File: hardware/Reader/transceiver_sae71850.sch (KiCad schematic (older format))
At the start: 17 parts

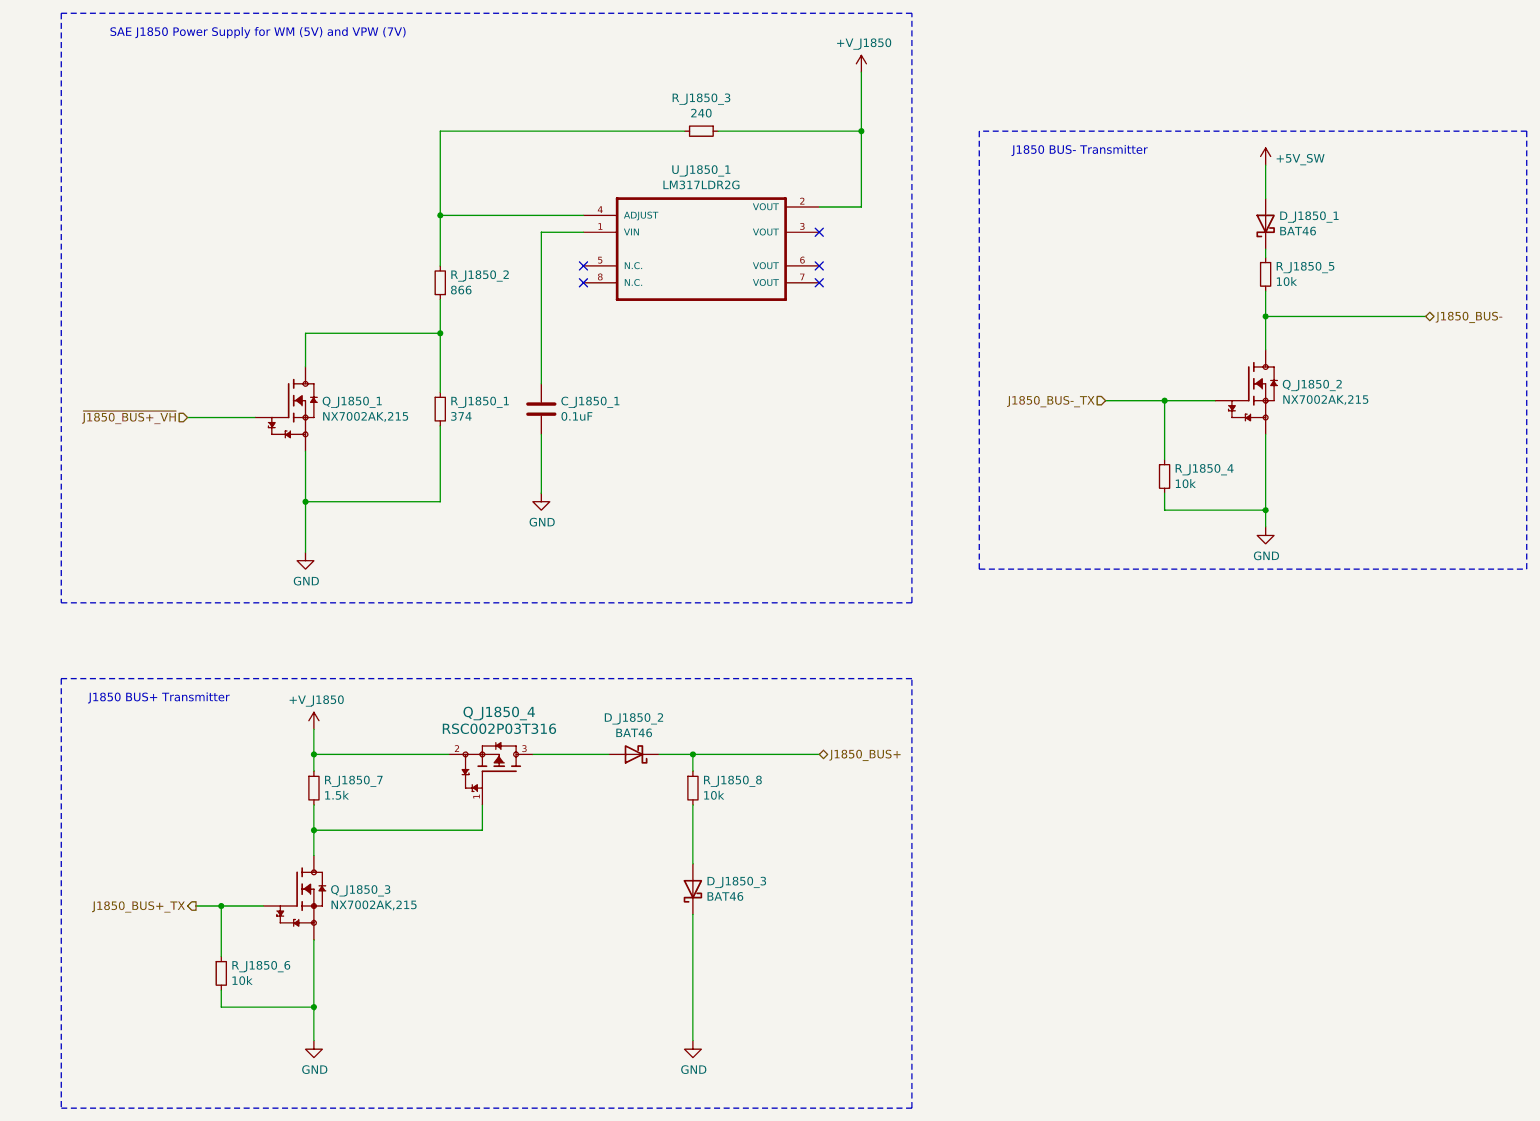
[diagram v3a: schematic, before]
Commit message: Fixed wiring issue on ESD Protection
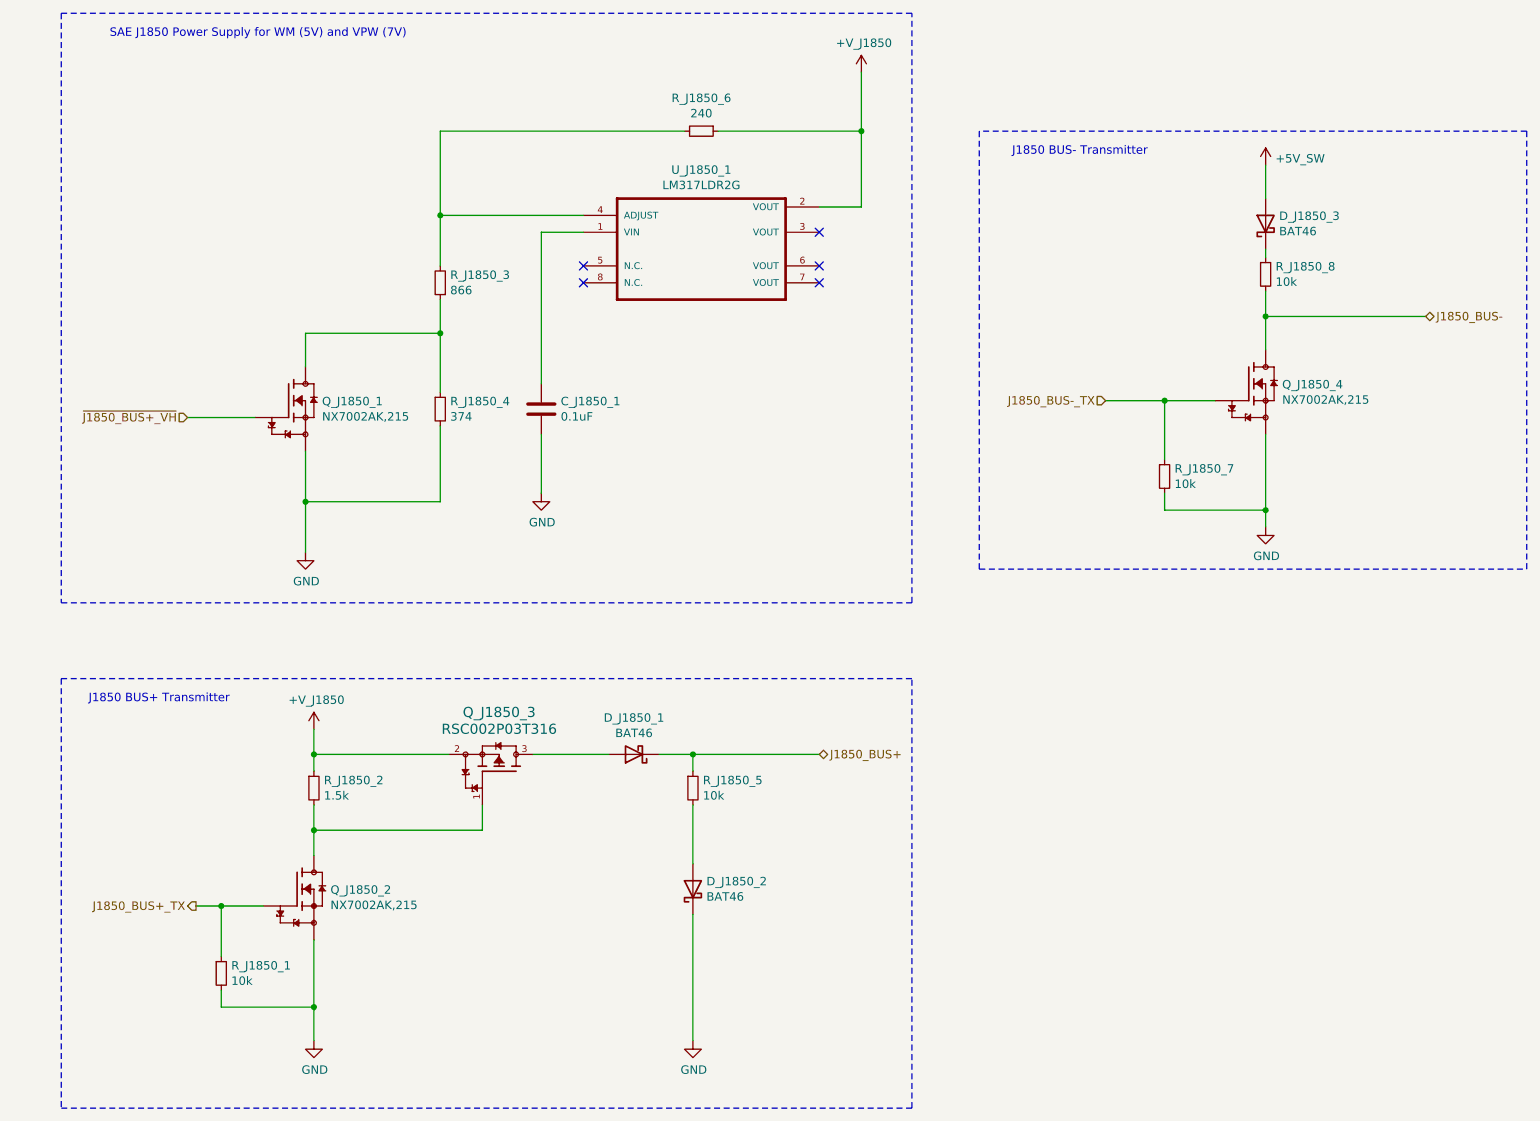
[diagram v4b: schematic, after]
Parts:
- renumbered D_J1850_2 to D_J1850_1, D_J1850_3 to D_J1850_2, D_J1850_1 to D_J1850_3, Q_J1850_3 to Q_J1850_2, Q_J1850_4 to Q_J1850_3, Q_J1850_2 to Q_J1850_4, R_J1850_6 to R_J1850_1, R_J1850_7 to R_J1850_2, R_J1850_2 to R_J1850_3, R_J1850_1 to R_J1850_4, R_J1850_8 to R_J1850_5, R_J1850_3 to R_J1850_6, R_J1850_4 to R_J1850_7, R_J1850_5 to R_J1850_8
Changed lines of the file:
@@
 $EndComp
 $Comp
-L power:GND #PWR0165
+L power:GND #PWR032
 U 1 1 5FB553C7
 P 3500 3550
-F 0 "#PWR0165" H 3500 3300 50  0001 C CNN
+F 0 "#PWR032" H 3500 3300 50  0001 C CNN
 F 1 "GND" H 3505 3377 50  0000 C CNN
 F 2 "" H 3500 3550 50  0001 C CNN
@@
 $EndComp
 $Comp
-L Device:R_Small R_J1850_3
+L Device:R_Small R_J1850_6
 U 1 1 5FB55A16
 P 4450 1400
-F 0 "R_J1850_3" V 4254 1400 50  0000 C CNN
+F 0 "R_J1850_6" V 4254 1400 50  0000 C CNN
 F 1 "240" V 4345 1400 50  0000 C CNN
 F 2 "footprints:RESC3216X70N" H 4450 1400 50  0001 C CNN
@@
 $EndComp
 $Comp
-L Device:R_Small R_J1850_2
+L Device:R_Small R_J1850_3
 U 1 1 5FB56090
 P 2900 2300
-F 0 "R_J1850_2" H 2841 2254 50  0000 R CNN
+F 0 "R_J1850_3" H 2841 2254 50  0000 R CNN
 F 1 "866" H 2841 2345 50  0000 R CNN
 F 2 "footprints:RESC3216X70N" H 2900 2300 50  0001 C CNN
@@
 $EndComp
 $Comp
-L Device:R_Small R_J1850_1
+L Device:R_Small R_J1850_4
 U 1 1 5FB59A27
 P 2900 3050
-F 0 "R_J1850_1" H 2959 3096 50  0000 L CNN
+F 0 "R_J1850_4" H 2959 3096 50  0000 L CNN
 F 1 "374" H 2959 3005 50  0000 L CNN
 F 2 "footprints:RESC3216X70N" H 2900 3050 50  0001 C CNN
@@
 	2900 3600 2900 3150
 $Comp
-L power:GND #PWR0166
+L power:GND #PWR029
 U 1 1 5FB5A98F
 P 2100 3900
-F 0 "#PWR0166" H 2100 3650 50  0001 C CNN
+F 0 "#PWR029" H 2100 3650 50  0001 C CNN
 F 1 "GND" H 2105 3727 50  0000 C CNN
 F 2 "" H 2100 3900 50  0001 C CNN
@@
 Connection ~ 2100 3600
 $Comp
-L CANtech:+V_J1850 #PWR0167
+L CANtech:+V_J1850 #PWR034
 U 1 1 5FB539A6
 P 5400 1050
-F 0 "#PWR0167" H 5400 900 50  0001 C CNN
+F 0 "#PWR034" H 5400 900 50  0001 C CNN
 F 1 "+V_J1850" H 5415 1223 50  0000 C CNN
 F 2 "" H 5400 1050 50  0001 C CNN
@@
 SAE J1850 Power Supply for WM (5V) and VPW (7V)
 $Comp
-L NX7002AK_215:NX7002AK,215 Q_J1850_3
+L NX7002AK_215:NX7002AK,215 Q_J1850_2
 U 1 1 5FB62A81
 P 2050 5900
-F 0 "Q_J1850_3" H 2248 5896 50  0000 L CNN
+F 0 "Q_J1850_2" H 2248 5896 50  0000 L CNN
 F 1 "NX7002AK,215" H 2248 5805 50  0000 L CNN
 F 2 "footprints:SOT95P230X110-3N" H 2050 5900 50  0001 L BNN
@@
 $EndComp
 $Comp
-L RSC002P03T316:RSC002P03T316 Q_J1850_4
+L RSC002P03T316:RSC002P03T316 Q_J1850_3
 U 1 1 5FB63A72
 P 3000 5450
-F 0 "Q_J1850_4" V 3600 5700 60  0000 C CNN
+F 0 "Q_J1850_3" V 3600 5700 60  0000 C CNN
 F 1 "RSC002P03T316" V 3500 5700 60  0000 C CNN
 F 2 "footprints:RSC002P03T316" H 3800 5690 60  0001 C CNN
@@
 $EndComp
 $Comp
-L Device:R_Small R_J1850_7
+L Device:R_Small R_J1850_2
 U 1 1 5FB64FDA
 P 2150 5300
-F 0 "R_J1850_7" H 2209 5346 50  0000 L CNN
+F 0 "R_J1850_2" H 2209 5346 50  0000 L CNN
 F 1 "1.5k" H 2209 5255 50  0000 L CNN
 F 2 "footprints:RESC1607X60N" H 2150 5300 50  0001 C CNN
@@
 	2150 5200 2150 5100
 $Comp
-L CANtech:+V_J1850 #PWR0168
+L CANtech:+V_J1850 #PWR030
 U 1 1 5FB735C3
 P 2150 4950
-F 0 "#PWR0168" H 2150 4800 50  0001 C CNN
+F 0 "#PWR030" H 2150 4800 50  0001 C CNN
 F 1 "+V_J1850" H 2165 5123 50  0000 C CNN
 F 2 "" H 2150 4950 50  0001 C CNN
@@
 J1850_BUS+_TX
 $Comp
-L Device:R_Small R_J1850_6
+L Device:R_Small R_J1850_1
 U 1 1 5FB73FCF
 P 1600 6400
-F 0 "R_J1850_6" H 1659 6446 50  0000 L CNN
+F 0 "R_J1850_1" H 1659 6446 50  0000 L CNN
 F 1 "10k" H 1659 6355 50  0000 L CNN
 F 2 "footprints:RESC1608X55N" H 1600 6400 50  0001 C CNN
@@
 $EndComp
 $Comp
-L power:GND #PWR0169
+L power:GND #PWR031
 U 1 1 5FB743BE
 P 2150 6800
-F 0 "#PWR0169" H 2150 6550 50  0001 C CNN
+F 0 "#PWR031" H 2150 6550 50  0001 C CNN
 F 1 "GND" H 2155 6627 50  0000 C CNN
 F 2 "" H 2150 6800 50  0001 C CNN
@@
 Connection ~ 2150 5100
 $Comp
-L Diode:BAT46 D_J1850_2
+L Diode:BAT46 D_J1850_1
 U 1 1 5FB795A0
 P 4050 5100
-F 0 "D_J1850_2" H 4050 4883 50  0000 C CNN
+F 0 "D_J1850_1" H 4050 4883 50  0000 C CNN
 F 1 "BAT46" H 4050 4974 50  0000 C CNN
 F 2 "Diode_THT:D_DO-35_SOD27_P7.62mm_Horizontal" H 4050 4925 50  0001 C CNN
@@
 	4200 5100 4400 5100
 $Comp
-L Device:R_Small R_J1850_8
+L Device:R_Small R_J1850_5
 U 1 1 5FB7CD86
 P 4400 5300
-F 0 "R_J1850_8" H 4459 5346 50  0000 L CNN
+F 0 "R_J1850_5" H 4459 5346 50  0000 L CNN
 F 1 "10k" H 4459 5255 50  0000 L CNN
 F 2 "footprints:RESC1608X55N" H 4400 5300 50  0001 C CNN
@@
 $EndComp
 $Comp
-L Diode:BAT46 D_J1850_3
+L Diode:BAT46 D_J1850_2
 U 1 1 5FB7D020
 P 4400 5900
-F 0 "D_J1850_3" V 4446 5820 50  0000 R CNN
+F 0 "D_J1850_2" V 4446 5820 50  0000 R CNN
 F 1 "BAT46" V 4355 5820 50  0000 R CNN
 F 2 "Diode_THT:D_DO-35_SOD27_P7.62mm_Horizontal" H 4400 5725 50  0001 C CNN
@@
 	4400 5400 4400 5750
 $Comp
-L power:GND #PWR0170
+L power:GND #PWR033
 U 1 1 5FB7EDB5
 P 4400 6800
-F 0 "#PWR0170" H 4400 6550 50  0001 C CNN
+F 0 "#PWR033" H 4400 6550 50  0001 C CNN
 F 1 "GND" H 4405 6627 50  0000 C CNN
 F 2 "" H 4400 6800 50  0001 C CNN
@@
 J1850_BUS-_TX
 $Comp
-L NX7002AK_215:NX7002AK,215 Q_J1850_2
+L NX7002AK_215:NX7002AK,215 Q_J1850_4
 U 1 1 5FB836A9
 P 7700 2900
-F 0 "Q_J1850_2" H 7898 2896 50  0000 L CNN
+F 0 "Q_J1850_4" H 7898 2896 50  0000 L CNN
 F 1 "NX7002AK,215" H 7898 2805 50  0000 L CNN
 F 2 "footprints:SOT95P230X110-3N" H 7700 2900 50  0001 L BNN
@@
 $EndComp
 $Comp
-L Device:R_Small R_J1850_4
+L Device:R_Small R_J1850_7
 U 1 1 5FB84DD1
 P 7200 3450
-F 0 "R_J1850_4" H 7259 3496 50  0000 L CNN
+F 0 "R_J1850_7" H 7259 3496 50  0000 L CNN
 F 1 "10k" H 7259 3405 50  0000 L CNN
 F 2 "footprints:RESC1608X55N" H 7200 3450 50  0001 C CNN
@@
 $EndComp
 $Comp
-L Device:R_Small R_J1850_5
+L Device:R_Small R_J1850_8
 U 1 1 5FB8513E
 P 7800 2250
-F 0 "R_J1850_5" H 7859 2296 50  0000 L CNN
+F 0 "R_J1850_8" H 7859 2296 50  0000 L CNN
 F 1 "10k" H 7859 2205 50  0000 L CNN
 F 2 "footprints:RESC1608X55N" H 7800 2250 50  0001 C CNN
@@
 $EndComp
 $Comp
-L Diode:BAT46 D_J1850_1
+L Diode:BAT46 D_J1850_3
 U 1 1 5FB86936
 P 7800 1950
-F 0 "D_J1850_1" V 7846 1870 50  0000 R CNN
+F 0 "D_J1850_3" V 7846 1870 50  0000 R CNN
 F 1 "BAT46" V 7755 1870 50  0000 R CNN
 F 2 "Diode_THT:D_DO-35_SOD27_P7.62mm_Horizontal" H 7800 1775 50  0001 C CNN
@@
 	7200 3000 7500 3000
 $Comp
-L power:GND #PWR0171
+L power:GND #PWR036
 U 1 1 5FB89303
 P 7800 3750
-F 0 "#PWR0171" H 7800 3500 50  0001 C CNN
+F 0 "#PWR036" H 7800 3500 50  0001 C CNN
 F 1 "GND" H 7805 3577 50  0000 C CNN
 F 2 "" H 7800 3750 50  0001 C CNN
@@
 	7800 2500 7800 2350
 $Comp
-L CANtech:+5V_SW #PWR0172
+L CANtech:+5V_SW #PWR035
 U 1 1 5FB8FBF4
 P 7800 1600
-F 0 "#PWR0172" H 7800 1850 50  0001 C CNN
+F 0 "#PWR035" H 7800 1850 50  0001 C CNN
 F 1 "+5V_SW" H 7858 1637 50  0000 L CNN
 F 2 "" H 7050 2400 50  0001 C CNN
